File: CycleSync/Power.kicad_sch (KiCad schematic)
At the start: 0 parts

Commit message: s
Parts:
- added C68, C69, C70, C71, C72, C73, C80, C81: 1u, symbol Device:C
- added C74: 33n, symbol Device:C
- added C75, C82: 10u, symbol Device:C
- added C76: 0u1, symbol Device:C
- added C77: 100n, symbol Device:C
- added C78, C79: 22u, symbol Device:C
- added L3: 4u7, symbol Device:L
- added Q2: 2N7002, Package_TO_SOT_SMD:SOT-23, symbol Transistor_FET:2N7002
- added R43, R48, R50: 100k, symbol Device:R
- added R44: 30.9k, symbol Device:R
- added R45, R47, R49: 10k, symbol Device:R
- added R46: 31R3, symbol Device:R
- added U10, U11: TPS7A2033PDBVR, Package_TO_SOT_SMD:SOT-23-5, symbol Regulator_Linear:TPS7A20xxxDBV
- added U12: TLV71211DBVR, Package_TO_SOT_SMD:SOT-23-5, symbol Regulator_Linear:TLV71211_SOT23-5
- added U8: TPS2116DRL, Package_TO_SOT_SMD:SOT-583-8, symbol Power_Management:TPS2116DRL
- added U9: TPS62932, Package_TO_SOT_SMD:SOT-583-8, symbol Regulator_Switching:TPS62932
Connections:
- new net: R46.2, R47.1, U9.8 (FB)
- new net: R43.2, R44.1, U8.4 (PR1)
- new net: C77.1, U9.6 (BST)
- new net: C77.2, L3.1, U9.5 (SW)
- new net: R45.2, U8.8 (ST)
- new net: Q2.1 (G), R49.2, R50.2
- new net: C74.2, U9.7 (SS)
- new net +1V1: C71.1, U12.5 (OUT)
- new net +3V3_AUDIO: C73.1, U10.5 (OUT)
- new net +3V3_DIG: C70.1, C78.1, C79.1, L3.2, R45.1, R46.1, U12.1 (IN), U12.3 (EN)
- new net +3V3_GNSS: C81.1, U11.5 (OUT)
- new net GND: C68.2, C69.2, C70.2, C71.2, C72.2, C73.2, C74.1, C75.2, C76.2, C78.2, C79.2, C80.2, C81.2, C82.2, Q2.2 (S), R44.2, R47.2, R50.1, U10.2 (GND), U11.2 (GND), U12.2 (GND), U8.1 (GND), U9.4 (GND)
- new net GNSS_LDO_EN: Q2.3 (D), R48.2, U11.3 (EN)
- new net GNSS_VCC_CUTOFF: R49.1
- new net PP5V: C72.1, C75.1, C76.1, C80.1, C82.1, R48.1, U10.1 (IN), U10.3 (EN), U11.1 (IN), U8.2 (VOUT), U8.7 (VOUT), U9.3 (VIN)
- new net VBUS_HOST_5V: C69.1, U8.6 (VIN2)
- new net VBUS_PD_5V: C68.1, R43.1, U8.3 (VIN1), U8.5 (MODE)
- no-connect marks 0 -> 2
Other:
- note added: "+1.1 V MCU CORE LDO"
- note added: "+3.3 V AUDIO ANALOG LDO"
- note added: "DUAL-VBUS POWER MUX & +5 V SYSTEM RAIL"
- note added: "GNSS POWER CUTOFF & +3.3 V GNSS LDO"
- note added: "MAIN +3.3 V DIGITAL BUCK"
- title: (none) -> SYSTEM POWER TREE & RAIL GENERATION

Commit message: verified schematic wirings
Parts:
- added C71: 1u, symbol Device:C
- added C72: 10n, symbol Device:C
- added D6: 1N4148WS, symbol Device:D_Small
- added R48: 100k, symbol Device:R
- added U11: TPS22918DBVR, Package_TO_SOT_SMD:SOT-23-6, symbol CycleSync_local:TPS22918DBV
- R52: renamed from R46; value 31R3 -> 31k3
- renumbered C68 to C69, C82 to C70, C69 to C73, C70 to C74, C71 to C75, C72 to C76, C73 to C77, C75 to C78, C76 to C79, C74 to C80, C77 to C81, C78 to C82, C79 to C83, C80 to C84, C81 to C85, R43 to R45, R44 to R46, R45 to R47, R48 to R49, R49 to R50, R50 to R51, R47 to R53, U8 to U10, U10 to U13, U9 to U15, U11 to U16
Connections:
- net GND: now also C71.2, C72.1, U11.2 (GND)
- net VBUS_HOST_5V: now also D6.1 (K), R48.2, U11.1 (VIN); no longer U10.6 (VIN2)
- new net HOST_SW_CT: C72.2, U11.4 (CT)
- new net HOST_SW_ON: C71.1, D6.2 (A), R48.1, U11.3 (ON)
- new net VBUS_HOST_LIMITED_5V: U10.6 (VIN2), U11.6 (VOUT)
- no-connect marks 2 -> 3
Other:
- note added: "+3V3_DIG SETPOINT VOUT = 0.8 × (1 + R52/R53) = 0.8 × (1 + 31.3k/10k) ≈ 3.304 V NOMINAL."
- note added: "Firmware Note PHONE-POWERED FALLBACK USES U11 DIRECT VBUS PATH. TPS25751 PPHV SINK PATH MUST REMAIN DISABLED IN THIS MODE."
- note added: "HOST VBUS INRUSH LIMITER U11 OUTPUT RAMP ≈ 26.6 ms WITH C72 = 10 nF. R48/C71 DELAY ENABLE. D6 RAPIDLY RESETS THE DELAY AFTER UNPLUG. QOD IS INTENTIONALLY LEFT OPEN. U11 LIMITS THE DIRECT HOST-VBUS PATH. THE EXTERNAL 5 V INPUT BYPASSES U11."
- note added: "TPS2116 INPUT PRIORITY VIN1 = VBUS_PD_5V VIN2 = VBUS_HOST_LIMITED_5V MODE IS TIED TO VIN1. R45 = 100 kΩ, R46 = 30.9 kΩ: VIN1 SWITCHOVER THRESHOLD ≈ 4.24 V TYP. ST IS OPEN-DRAIN; R47 = 10 kΩ PULL-UP."
- moved on the sheet: C69, C70, C73, C74, C75, R45, R46, R47, U10, U12

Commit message: added some new testpoints for I2C
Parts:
- added TP19: +1V1, TestPoint:TestPoint_Pad_D1.5mm, symbol Connector:TestPoint
- added TP20: +3V3_AUDIO, TestPoint:TestPoint_Pad_D1.5mm, symbol Connector:TestPoint
- C69, C71, C73, C74, C75, C76, C77, C84, C85: footprint (none) -> Capacitor_SMD:C_0603_1608Metric
- C70, C78: footprint (none) -> Capacitor_SMD:C_0805_2012Metric
- C72, C79, C80, C81: footprint (none) -> Capacitor_SMD:C_0402_1005Metric
- C82, C83: footprint (none) -> Capacitor_SMD:C_1206_3216Metric
- D6: footprint (none) -> Diode_SMD:D_SOD-323
- R45, R46, R52, R53: footprint (none) -> Resistor_SMD:R_0603_1608Metric
- R47, R48, R49, R50, R51: footprint (none) -> Resistor_SMD:R_0402_1005Metric
- renumbered U15 to U14, U16 to U15
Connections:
- net +1V1: now also TP19.1
- net +3V3_AUDIO: now also TP20.1

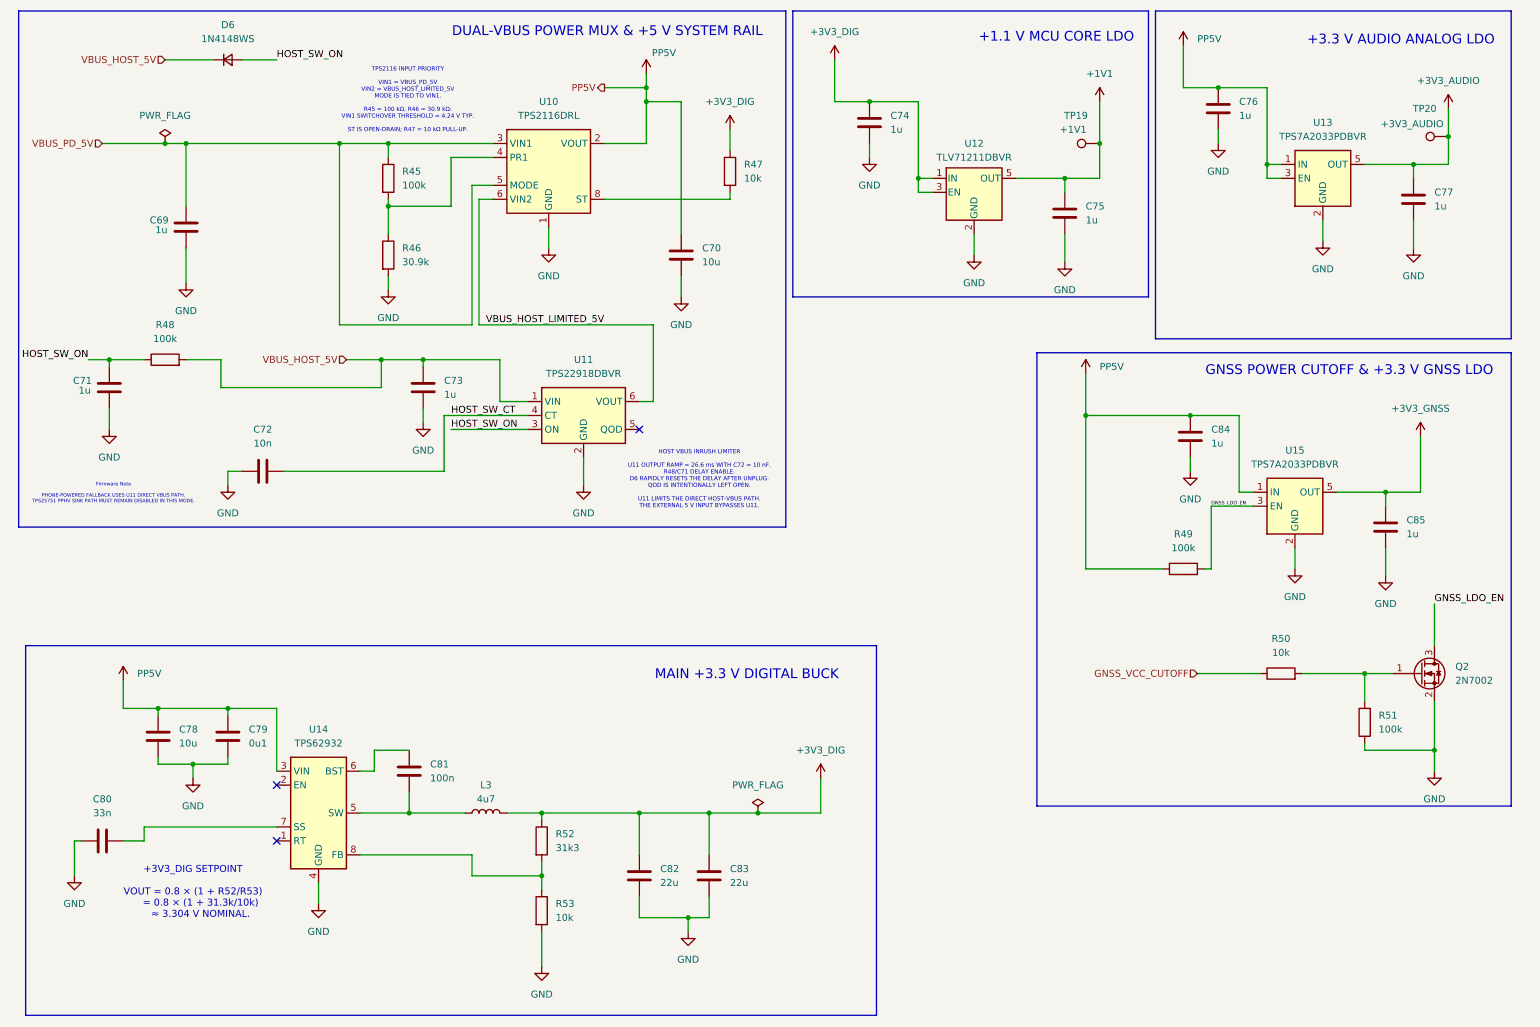
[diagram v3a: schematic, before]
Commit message: added footprints and manufacturer part number
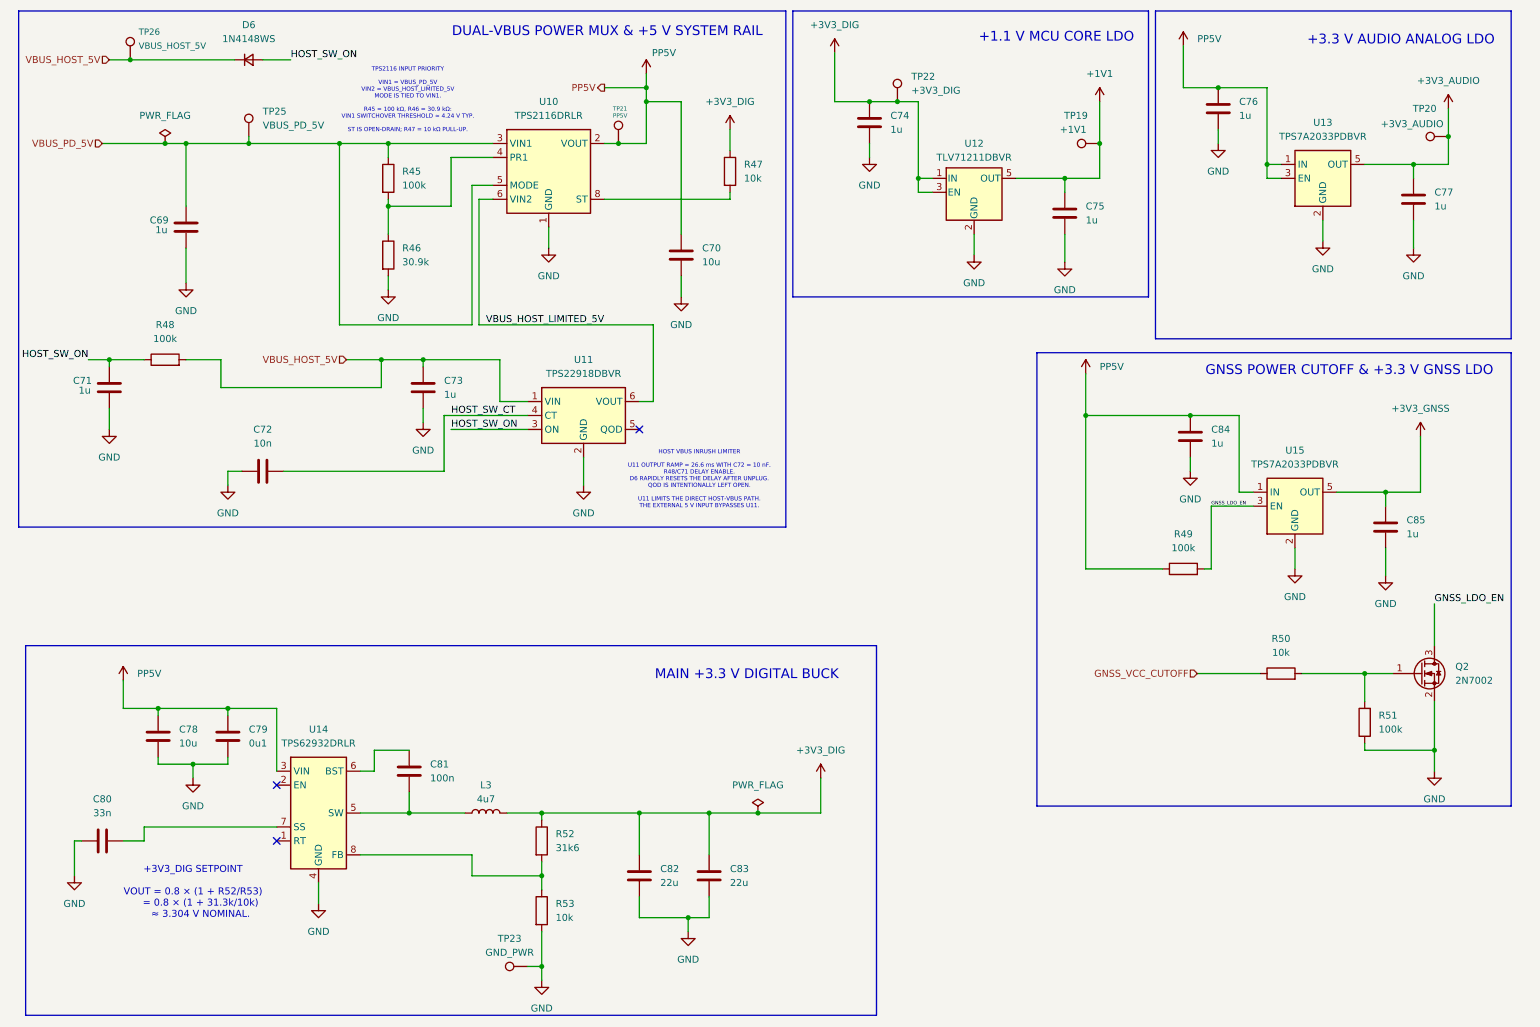
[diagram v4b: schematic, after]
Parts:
- added TP21: PP5V, TestPoint:TestPoint_Pad_D1.5mm, symbol Connector:TestPoint
- added TP22: +3V3_DIG, TestPoint:TestPoint_Pad_D1.5mm, symbol Connector:TestPoint
- added TP23: GND_PWR, TestPoint:TestPoint_Pad_D1.5mm, symbol Connector:TestPoint
- added TP25: VBUS_PD_5V, TestPoint:TestPoint_Pad_D1.5mm, symbol Connector:TestPoint
- added TP26: VBUS_HOST_5V, TestPoint:TestPoint_Pad_D1.5mm, symbol Connector:TestPoint
- C69, C71, C73, C74, C75, C76, C77, C84, C85: Distributor Link (none) -> https://jlcpcb.com/partdetail/30690-CL10B105KA8NNNC/C29936; MANUFACTURER (none) -> Samsung Electro-Mechanics; MPN (none) -> CL10B105KA8NNNC
- C70, C78: Distributor Link (none) -> https://jlcpcb.com/partdetail/236937-GRM21BZ71E106KE15L/C23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; MANUFACTURER (none) -> Murata Electronics; MPN (none) -> GRM21BZ71E106KE15L
- C72: Distributor Link (none) -> https://jlcpcb.com/partdetail/4423878-GRM1555C1E103JE01D/C3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; MANUFACTURER (none) -> Murata Electronics; MPN (none) -> GRM1555C1E103JE01D
- C79: Distributor Link (none) -> https://jlcpcb.com/partdetail/291005-CL05B104KB54PNC/C307331; MANUFACTURER (none) -> Samsung Electro-Mechanics; MPN (none) -> CL05B104KB54PNC
- C80: Distributor Link (none) -> https://jlcpcb.com/partdetail/196450-GCM155R71E333KA55D/C18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; MANUFACTURER (none) -> Murata Electronics; MPN (none) -> GCM155R71E333KA55D
- C81: Distributor Link (none) -> https://jlcpcb.com/partdetail/MurataElectronics-GRM155R71A1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; MANUFACTURER (none) -> Murata Electronics; MPN (none) -> GRM155R71A104KA01D
- C82, C83: Distributor Link (none) -> https://jlcpcb.com/partdetail/13537-CL31A226KAHNNNE/C12891; MANUFACTURER (none) -> Samsung Electro-Mechanics; MPN (none) -> CL31A226KAHNNNE
- D6: Distributor Link (none) -> https://jlcpcb.com/partdetail/onsemi-1N4148WS/C118873; MANUFACTURER (none) -> onsemi; MPN (none) -> 1N4148WS
- L3: footprint (none) -> Inductor_SMD:L_Sunlord_SWPA5040S; Distributor Link (none) -> https://jlcpcb.com/partdetail/Sunlord-SWPA5040S4R7MT/C48496; MANUFACTURER (none) -> Sunlord; MPN (none) -> SWPA5040S4R7MT
- Q2: Distributor Link (none) -> https://jlcpcb.com/partdetail/JSCJ-2N7002/C8545; MANUFACTURER (none) -> Jiangsu Changjing Electronics Technology Co., Ltd.; MPN (none) -> 2N7002
- R45: Distributor Link (none) -> https://jlcpcb.com/partdetail/26546-0603WAF1003T5E/C25803; MANUFACTURER (none) -> UNI-ROYAL(Uniroyal Elec); MPN (none) -> 0603WAF1003T5E
- R46: Distributor Link (none) -> https://jlcpcb.com/partdetail/23749-0603WAF3092T5E/C23022; MANUFACTURER (none) -> UNI-ROYAL(Uniroyal Elec); MPN (none) -> 0603WAF3092T5E
- R47, R50: Distributor Link (none) -> https://jlcpcb.com/partdetail/YAGEO-RC0402FR0710KL/C60490; MANUFACTURER (none) -> YAGEO; MPN (none) -> RC0402FR-0710KL
- R48, R49, R51: Distributor Link (none) -> https://jlcpcb.com/partdetail/YAGEO-RC0402FR07100KL/C60491; MANUFACTURER (none) -> YAGEO; MPN (none) -> RC0402FR-07100KL
- R52: value 31k3 -> 31k6; Distributor Link (none) -> https://jlcpcb.com/partdetail/26710-0603WAF3162T5E/C25967; MANUFACTURER (none) -> UNI-ROYAL(Uniroyal Elec); MPN (none) -> 0603WAF3162T5E
- R53: Distributor Link (none) -> https://jlcpcb.com/partdetail/YAGEO-RC0603FR0710KL/C98220; MANUFACTURER (none) -> YAGEO; MPN (none) -> RC0603FR-0710KL
- TP19, TP20: now left out of the parts list
- U10: value TPS2116DRL -> TPS2116DRLR; Distributor Link (none) -> https://jlcpcb.com/partdetail/TexasInstruments-TPS2116DRLR/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; MANUFACTURER (none) -> Texas Instruments; MPN (none) -> TPS2116DRLR
- U11: Distributor Link (none) -> https://jlcpcb.com/partdetail/TexasInstruments-TPS22918DBVR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; MANUFACTURER (none) -> Texas Instruments; MPN (none) -> TPS22918DBVR
- U12: Distributor Link (none) -> https://jlcpcb.com/partdetail/TexasInstruments-TLV71211DBVR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; MANUFACTURER (none) -> Texas Instruments; MPN (none) -> TLV71211DBVR
- U13, U15: Distributor Link (none) -> https://jlcpcb.com/partdetail/TexasInstruments-TPS7A2033PDB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; MANUFACTURER (none) -> Texas Instruments; MPN (none) -> TPS7A2033PDBVR
- U14: value TPS62932 -> TPS62932DRLR; Distributor Link (none) -> https://jlcpcb.com/partdetail/TexasInstruments-TPS62932DRLR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; MANUFACTURER (none) -> Texas Instruments; MPN (none) -> TPS62932DRLR
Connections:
- net +3V3_DIG: now also TP22.1
- net GND: now also TP23.1
- net PP5V: now also TP21.1
- net VBUS_HOST_5V: now also TP26.1
- net VBUS_PD_5V: now also TP25.1
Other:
- note removed: "Firmware Note PHONE-POWERED FALLBACK USES U11 DIRECT VBUS PATH. TPS25751 PPHV SINK PATH MUST REMAIN DISABLED IN THIS MODE."
- moved on the sheet: D6
